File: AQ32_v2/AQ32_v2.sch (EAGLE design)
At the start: 115 parts, among them Q2 BCV27, Q3 BCV27, Q5 BCV27, Q6 BCV27, U1 ITG-3200, U10 MS5611, U11 MIC5239, U13 74AHC1G86DCK, U2 STM32F10XVXT6, U3 74AHC1G86DCK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

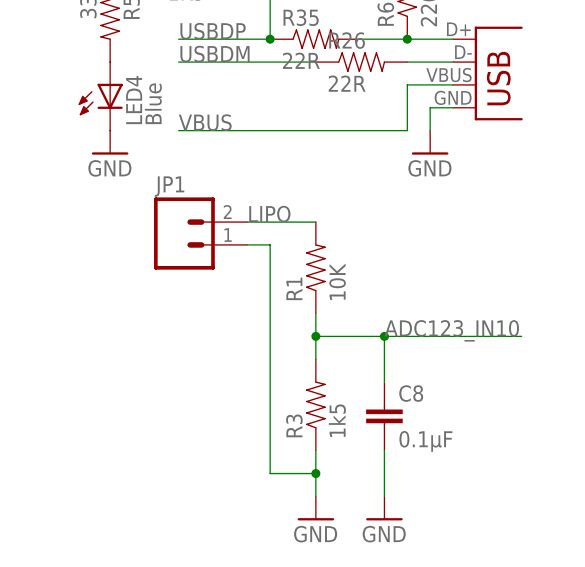
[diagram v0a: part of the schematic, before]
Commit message: reverted to fixed ground plane for BM and LED GND's, moved lavels
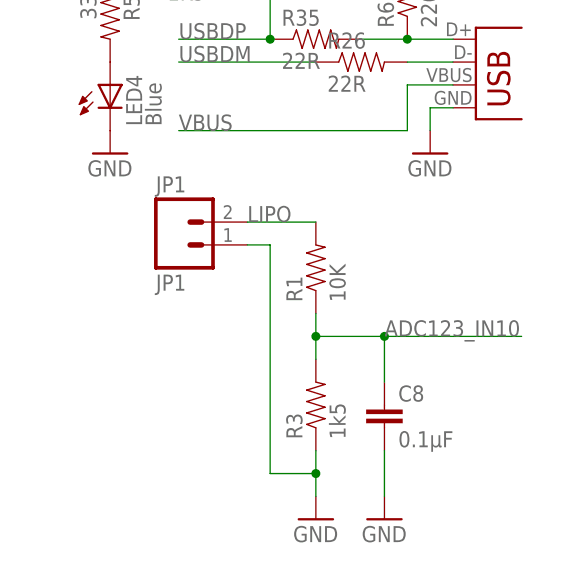
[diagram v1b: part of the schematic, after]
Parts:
- JP1: value (none) -> JP1; device SparkFun-Connectors:M02PTH -> SparkFun-Connectors:M02LOCK
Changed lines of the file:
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@@
 <part name="GND25" library="SparkFun" deviceset="GND" device=""/>
 <part name="SUPPLY2" library="supply2" deviceset="V+" device="" value="VDD"/>
-<part name="JP1" library="SparkFun-Connectors" deviceset="M02" device="PTH"/>
+<part name="JP1" library="SparkFun-Connectors" deviceset="M02" device="LOCK" value="JP1"/>
 </parts>
 <sheets>
@@
 <pinref part="R3" gate="G$1" pin="1"/>
 <pinref part="GND15" gate="1" pin="GND"/>
-<pinref part="JP1" gate="G$1" pin="1"/>
 <wire x1="33.02" y1="73.66" x2="33.02" y2="71.12" width="0.1524" layer="91"/>
 <wire x1="25.4" y1="99.06" x2="27.94" y2="99.06" width="0.1524" layer="91"/>
@@
 <wire x1="27.94" y1="73.66" x2="33.02" y2="73.66" width="0.1524" layer="91"/>
 <junction x="33.02" y="73.66"/>
-</segment>
-<segment>
+<pinref part="JP1" gate="G$1" pin="1"/>
+</segment>
+<segment>

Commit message: "j" version from Alfred
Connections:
- net 3V3AN: now also C29.1, C45.1, U1.VDD, U10.CSB, U10.CSB@2, U10.PS, U10.VDD; no longer I2C-1.S, JP1-2.7, JP1-2.8, SERIAL-1.S
- net 3V3DIG: now also I2C-1.S, JP1-2.7, JP1-2.8, SERIAL-1.S; no longer C29.1, C45.1, U1.VDD, U10.CSB, U10.CSB@2, U10.PS, U10.VDD
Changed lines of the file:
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@@
 <part name="U10" library="DSP-TI" deviceset="MS5611" device=""/>
 <part name="SUPPLY19" library="supply2" deviceset="GND" device=""/>
-<part name="SUPPLY20" library="supply2" deviceset="VDD" device=""/>
 <part name="C45" library="rcl" deviceset="C-US" device="C0402" value="0.1uF"/>
 <part name="SUPPLY21" library="supply2" deviceset="GND" device=""/>
@@
 <part name="SUPPLY2" library="supply2" deviceset="V+" device="" value="VDD"/>
 <part name="JP1" library="SparkFun-Connectors" deviceset="M02" device="LOCK" value="JP1"/>
+<part name="P+4" library="SparkFun" deviceset="3.3V" device="" value="VDDA"/>
 </parts>
 <sheets>
@@
 <instance part="U10" gate="G$1" x="307.34" y="33.02"/>
 <instance part="SUPPLY19" gate="GND" x="309.88" y="10.16"/>
-<instance part="SUPPLY20" gate="G$1" x="309.88" y="60.96"/>
 <instance part="C45" gate="G$1" x="325.12" y="50.8"/>
 <instance part="SUPPLY21" gate="GND" x="325.12" y="40.64"/>
@@
 <instance part="SUPPLY2" gate="1" x="129.54" y="60.96"/>
 <instance part="JP1" gate="G$1" x="17.78" y="99.06"/>
+<instance part="P+4" gate="G$1" x="309.88" y="58.42"/>
 </instances>
 <busses>
@@
 </segment>
 <segment>
-<pinref part="SERIAL" gate="-1" pin="S"/>
-<wire x1="86.36" y1="68.58" x2="76.2" y2="68.58" width="0.1524" layer="91"/>
-<label x="76.2" y="68.58" size="1.778" layer="95"/>
-</segment>
-<segment>
-<pinref part="I2C" gate="-1" pin="S"/>
-<wire x1="86.36" y1="83.82" x2="76.2" y2="83.82" width="0.1524" layer="91"/>
-<label x="76.2" y="83.82" size="1.778" layer="95"/>
-</segment>
-<segment>
-<pinref part="JP1-2" gate="G$1" pin="8"/>
-<wire x1="429.26" y1="76.2" x2="436.88" y2="76.2" width="0.1524" layer="91"/>
-<label x="429.26" y="76.2" size="1.778" layer="95"/>
-</segment>
-<segment>
-<pinref part="JP1-2" gate="G$1" pin="7"/>
-<wire x1="429.26" y1="73.66" x2="436.88" y2="73.66" width="0.1524" layer="91"/>
-<label x="429.26" y="73.66" size="1.778" layer="95"/>
+<wire x1="309.88" y1="58.42" x2="309.88" y2="55.88" width="0.1524" layer="91"/>
+<wire x1="309.88" y1="55.88" x2="309.88" y2="50.8" width="0.1524" layer="91"/>
+<wire x1="309.88" y1="55.88" x2="325.12" y2="55.88" width="0.1524" layer="91"/>
+<wire x1="325.12" y1="55.88" x2="325.12" y2="53.34" width="0.1524" layer="91"/>
+<junction x="309.88" y="55.88"/>
+<pinref part="U10" gate="G$1" pin="VDD"/>
+<pinref part="C45" gate="G$1" pin="1"/>
+<label x="309.88" y="58.42" size="1.778" layer="95"/>
+<wire x1="309.88" y1="55.88" x2="281.94" y2="55.88" width="0.1524" layer="91"/>
+<wire x1="281.94" y1="55.88" x2="281.94" y2="40.64" width="0.1524" layer="91"/>
+<pinref part="U10" gate="G$1" pin="CSB@2"/>
+<wire x1="281.94" y1="40.64" x2="281.94" y2="38.1" width="0.1524" layer="91"/>
+<wire x1="281.94" y1="38.1" x2="281.94" y2="35.56" width="0.1524" layer="91"/>
+<wire x1="281.94" y1="35.56" x2="292.1" y2="35.56" width="0.1524" layer="91"/>
+<pinref part="U10" gate="G$1" pin="CSB"/>
+<wire x1="292.1" y1="38.1" x2="281.94" y2="38.1" width="0.1524" layer="91"/>
+<pinref part="U10" gate="G$1" pin="PS"/>
+<wire x1="292.1" y1="40.64" x2="281.94" y2="40.64" width="0.1524" layer="91"/>
+<junction x="281.94" y="40.64"/>
+<junction x="281.94" y="38.1"/>
+<pinref part="P+4" gate="G$1" pin="3.3V"/>
+</segment>
+<segment>
+<wire x1="342.9" y1="157.48" x2="327.66" y2="157.48" width="0.1524" layer="91"/>
+<wire x1="342.9" y1="157.48" x2="342.9" y2="149.86" width="0.1524" layer="91"/>
+<junction x="327.66" y="157.48"/>
+<label x="330.2" y="157.48" size="1.778" layer="95"/>
+<pinref part="U1" gate="G$1" pin="VDD"/>
+<pinref part="C29" gate="G$1" pin="1"/>
 </segment>
 </net>
@@
 </segment>
 <segment>
-<wire x1="309.88" y1="58.42" x2="309.88" y2="55.88" width="0.1524" layer="91"/>
-<wire x1="309.88" y1="55.88" x2="309.88" y2="50.8" width="0.1524" layer="91"/>
-<wire x1="309.88" y1="55.88" x2="325.12" y2="55.88" width="0.1524" layer="91"/>
-<wire x1="325.12" y1="55.88" x2="325.12" y2="53.34" width="0.1524" layer="91"/>
-<junction x="309.88" y="55.88"/>
-<pinref part="SUPPLY20" gate="G$1" pin="VDD"/>
-<pinref part="U10" gate="G$1" pin="VDD"/>
-<pinref part="C45" gate="G$1" pin="1"/>
-<label x="309.88" y="58.42" size="1.778" layer="95"/>
-<wire x1="309.88" y1="55.88" x2="281.94" y2="55.88" width="0.1524" layer="91"/>
-<wire x1="281.94" y1="55.88" x2="281.94" y2="40.64" width="0.1524" layer="91"/>
-<pinref part="U10" gate="G$1" pin="CSB@2"/>
-<wire x1="281.94" y1="40.64" x2="281.94" y2="38.1" width="0.1524" layer="91"/>
-<wire x1="281.94" y1="38.1" x2="281.94" y2="35.56" width="0.1524" layer="91"/>
-<wire x1="281.94" y1="35.56" x2="292.1" y2="35.56" width="0.1524" layer="91"/>
-<pinref part="U10" gate="G$1" pin="CSB"/>
-<wire x1="292.1" y1="38.1" x2="281.94" y2="38.1" width="0.1524" layer="91"/>
-<pinref part="U10" gate="G$1" pin="PS"/>
-<wire x1="292.1" y1="40.64" x2="281.94" y2="40.64" width="0.1524" layer="91"/>
-<junction x="281.94" y="40.64"/>
-<junction x="281.94" y="38.1"/>
-</segment>
-<segment>
-<wire x1="342.9" y1="157.48" x2="327.66" y2="157.48" width="0.1524" layer="91"/>
-<wire x1="342.9" y1="157.48" x2="342.9" y2="149.86" width="0.1524" layer="91"/>
-<junction x="327.66" y="157.48"/>
-<label x="330.2" y="157.48" size="1.778" layer="95"/>
-<pinref part="U1" gate="G$1" pin="VDD"/>
-<pinref part="C29" gate="G$1" pin="1"/>
-</segment>
-<segment>
 <wire x1="261.62" y1="170.18" x2="261.62" y2="175.26" width="0.1524" layer="91"/>
 <label x="259.08" y="175.26" size="1.778" layer="95"/>
@@
 <label x="129.54" y="55.88" size="1.778" layer="95"/>
 </segment>
-</net>
+<segment>
+<pinref part="I2C" gate="-1" pin="S"/>
+<wire x1="86.36" y1="83.82" x2="76.2" y2="83.82" width="0.1524" layer="91"/>
+<label x="76.2" y="83.82" size="1.778" layer="95"/>
+</segment>
+<segment>
+<pinref part="SERIAL" gate="-1" pin="S"/>
+<wire x1="86.36" y1="68.58" x2="76.2" y2="68.58" width="0.1524" layer="91"/>
+<label x="76.2" y="68.58" size="1.778" layer="95"/>
+</segment>
+<segment>
+<pinref part="JP1-2" gate="G$1" pin="8"/>
+<wire x1="429.26" y1="76.2" x2="436.88" y2="76.2" width="0.1524" layer="91"/>
+<label x="429.26" y="76.2" size="1.778" layer="95"/>
+</segment>
+<segment>
+<pinref part="JP1-2" gate="G$1" pin="7"/>
+<wire x1="429.26" y1="73.66" x2="436.88" y2="73.66" width="0.1524" layer="91"/>
+<label x="429.26" y="73.66" size="1.778" layer="95"/>
+</segment>
+</net>

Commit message: Revert ""j" version from Alfred"
This reverts commit dfbd99c4a951c4a7fc19233cae0e41e3843b112f.
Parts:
- JP1: value JP1 -> (none); device SparkFun-Connectors:M02LOCK -> SparkFun-Connectors:M02PTH
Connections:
- net 3V3AN: now also I2C-1.S, JP1-2.7, JP1-2.8, SERIAL-1.S; no longer C29.1, C45.1, U1.VDD, U10.CSB, U10.CSB@2, U10.PS, U10.VDD
- net 3V3DIG: now also C29.1, C45.1, U1.VDD, U10.CSB, U10.CSB@2, U10.PS, U10.VDD; no longer I2C-1.S, JP1-2.7, JP1-2.8, SERIAL-1.S
- net LEDGND1: now also Q5.C; no longer Q2.C
- net LEDGND2: now also Q2.C; no longer Q5.C
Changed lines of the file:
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@@
 <part name="U10" library="DSP-TI" deviceset="MS5611" device=""/>
 <part name="SUPPLY19" library="supply2" deviceset="GND" device=""/>
+<part name="SUPPLY20" library="supply2" deviceset="VDD" device=""/>
 <part name="C45" library="rcl" deviceset="C-US" device="C0402" value="0.1uF"/>
 <part name="SUPPLY21" library="supply2" deviceset="GND" device=""/>
@@
 <part name="GND25" library="SparkFun" deviceset="GND" device=""/>
 <part name="SUPPLY2" library="supply2" deviceset="V+" device="" value="VDD"/>
-<part name="JP1" library="SparkFun-Connectors" deviceset="M02" device="LOCK" value="JP1"/>
-<part name="P+4" library="SparkFun" deviceset="3.3V" device="" value="VDDA"/>
+<part name="JP1" library="SparkFun-Connectors" deviceset="M02" device="PTH"/>
 </parts>
 <sheets>
@@
 <instance part="U10" gate="G$1" x="307.34" y="33.02"/>
 <instance part="SUPPLY19" gate="GND" x="309.88" y="10.16"/>
+<instance part="SUPPLY20" gate="G$1" x="309.88" y="60.96"/>
 <instance part="C45" gate="G$1" x="325.12" y="50.8"/>
 <instance part="SUPPLY21" gate="GND" x="325.12" y="40.64"/>
@@
 <instance part="SUPPLY2" gate="1" x="129.54" y="60.96"/>
 <instance part="JP1" gate="G$1" x="17.78" y="99.06"/>
-<instance part="P+4" gate="G$1" x="309.88" y="58.42"/>
 </instances>
 <busses>
@@
 <pinref part="R3" gate="G$1" pin="1"/>
 <pinref part="GND15" gate="1" pin="GND"/>
+<pinref part="JP1" gate="G$1" pin="1"/>
 <wire x1="33.02" y1="73.66" x2="33.02" y2="71.12" width="0.1524" layer="91"/>
 <wire x1="25.4" y1="99.06" x2="27.94" y2="99.06" width="0.1524" layer="91"/>
@@
 <wire x1="27.94" y1="73.66" x2="33.02" y2="73.66" width="0.1524" layer="91"/>
 <junction x="33.02" y="73.66"/>
-<pinref part="JP1" gate="G$1" pin="1"/>
 </segment>
 <segment>
@@
 </segment>
 <segment>
-<wire x1="309.88" y1="58.42" x2="309.88" y2="55.88" width="0.1524" layer="91"/>
-<wire x1="309.88" y1="55.88" x2="309.88" y2="50.8" width="0.1524" layer="91"/>
-<wire x1="309.88" y1="55.88" x2="325.12" y2="55.88" width="0.1524" layer="91"/>
-<wire x1="325.12" y1="55.88" x2="325.12" y2="53.34" width="0.1524" layer="91"/>
-<junction x="309.88" y="55.88"/>
-<pinref part="U10" gate="G$1" pin="VDD"/>
-<pinref part="C45" gate="G$1" pin="1"/>
-<label x="309.88" y="58.42" size="1.778" layer="95"/>
-<wire x1="309.88" y1="55.88" x2="281.94" y2="55.88" width="0.1524" layer="91"/>
-<wire x1="281.94" y1="55.88" x2="281.94" y2="40.64" width="0.1524" layer="91"/>
-<pinref part="U10" gate="G$1" pin="CSB@2"/>
-<wire x1="281.94" y1="40.64" x2="281.94" y2="38.1" width="0.1524" layer="91"/>
-<wire x1="281.94" y1="38.1" x2="281.94" y2="35.56" width="0.1524" layer="91"/>
-<wire x1="281.94" y1="35.56" x2="292.1" y2="35.56" width="0.1524" layer="91"/>
-<pinref part="U10" gate="G$1" pin="CSB"/>
-<wire x1="292.1" y1="38.1" x2="281.94" y2="38.1" width="0.1524" layer="91"/>
-<pinref part="U10" gate="G$1" pin="PS"/>
-<wire x1="292.1" y1="40.64" x2="281.94" y2="40.64" width="0.1524" layer="91"/>
-<junction x="281.94" y="40.64"/>
-<junction x="281.94" y="38.1"/>
-<pinref part="P+4" gate="G$1" pin="3.3V"/>
-</segment>
-<segment>
-<wire x1="342.9" y1="157.48" x2="327.66" y2="157.48" width="0.1524" layer="91"/>
-<wire x1="342.9" y1="157.48" x2="342.9" y2="149.86" width="0.1524" layer="91"/>
-<junction x="327.66" y="157.48"/>
-<label x="330.2" y="157.48" size="1.778" layer="95"/>
-<pinref part="U1" gate="G$1" pin="VDD"/>
-<pinref part="C29" gate="G$1" pin="1"/>
+<pinref part="SERIAL" gate="-1" pin="S"/>
+<wire x1="86.36" y1="68.58" x2="76.2" y2="68.58" width="0.1524" layer="91"/>
+<label x="76.2" y="68.58" size="1.778" layer="95"/>
+</segment>
+<segment>
+<pinref part="I2C" gate="-1" pin="S"/>
+<wire x1="86.36" y1="83.82" x2="76.2" y2="83.82" width="0.1524" layer="91"/>
+<label x="76.2" y="83.82" size="1.778" layer="95"/>
+</segment>
+<segment>
+<pinref part="JP1-2" gate="G$1" pin="8"/>
+<wire x1="429.26" y1="76.2" x2="436.88" y2="76.2" width="0.1524" layer="91"/>
+<label x="429.26" y="76.2" size="1.778" layer="95"/>
+</segment>
+<segment>
+<pinref part="JP1-2" gate="G$1" pin="7"/>
+<wire x1="429.26" y1="73.66" x2="436.88" y2="73.66" width="0.1524" layer="91"/>
+<label x="429.26" y="73.66" size="1.778" layer="95"/>
 </segment>
 </net>
@@
 </segment>
 <segment>
+<wire x1="309.88" y1="58.42" x2="309.88" y2="55.88" width="0.1524" layer="91"/>
+<wire x1="309.88" y1="55.88" x2="309.88" y2="50.8" width="0.1524" layer="91"/>
+<wire x1="309.88" y1="55.88" x2="325.12" y2="55.88" width="0.1524" layer="91"/>
+<wire x1="325.12" y1="55.88" x2="325.12" y2="53.34" width="0.1524" layer="91"/>
+<junction x="309.88" y="55.88"/>
+<pinref part="SUPPLY20" gate="G$1" pin="VDD"/>
+<pinref part="U10" gate="G$1" pin="VDD"/>
+<pinref part="C45" gate="G$1" pin="1"/>
+<label x="309.88" y="58.42" size="1.778" layer="95"/>
+<wire x1="309.88" y1="55.88" x2="281.94" y2="55.88" width="0.1524" layer="91"/>
+<wire x1="281.94" y1="55.88" x2="281.94" y2="40.64" width="0.1524" layer="91"/>
+<pinref part="U10" gate="G$1" pin="CSB@2"/>
+<wire x1="281.94" y1="40.64" x2="281.94" y2="38.1" width="0.1524" layer="91"/>
+<wire x1="281.94" y1="38.1" x2="281.94" y2="35.56" width="0.1524" layer="91"/>
+<wire x1="281.94" y1="35.56" x2="292.1" y2="35.56" width="0.1524" layer="91"/>
+<pinref part="U10" gate="G$1" pin="CSB"/>
+<wire x1="292.1" y1="38.1" x2="281.94" y2="38.1" width="0.1524" layer="91"/>
+<pinref part="U10" gate="G$1" pin="PS"/>
+<wire x1="292.1" y1="40.64" x2="281.94" y2="40.64" width="0.1524" layer="91"/>
+<junction x="281.94" y="40.64"/>
+<junction x="281.94" y="38.1"/>
+</segment>
+<segment>
+<wire x1="342.9" y1="157.48" x2="327.66" y2="157.48" width="0.1524" layer="91"/>
+<wire x1="342.9" y1="157.48" x2="342.9" y2="149.86" width="0.1524" layer="91"/>
+<junction x="327.66" y="157.48"/>
+<label x="330.2" y="157.48" size="1.778" layer="95"/>
+<pinref part="U1" gate="G$1" pin="VDD"/>
+<pinref part="C29" gate="G$1" pin="1"/>
+</segment>
+<segment>
 <wire x1="261.62" y1="170.18" x2="261.62" y2="175.26" width="0.1524" layer="91"/>
 <label x="259.08" y="175.26" size="1.778" layer="95"/>
@@
 <pinref part="U3" gate="P" pin="VCC"/>
 <label x="129.54" y="55.88" size="1.778" layer="95"/>
-</segment>
-<segment>
-<pinref part="I2C" gate="-1" pin="S"/>
-<wire x1="86.36" y1="83.82" x2="76.2" y2="83.82" width="0.1524" layer="91"/>
-<label x="76.2" y="83.82" size="1.778" layer="95"/>
-</segment>
-<segment>
-<pinref part="SERIAL" gate="-1" pin="S"/>
-<wire x1="86.36" y1="68.58" x2="76.2" y2="68.58" width="0.1524" layer="91"/>
-<label x="76.2" y="68.58" size="1.778" layer="95"/>
-</segment>
-<segment>
-<pinref part="JP1-2" gate="G$1" pin="8"/>
-<wire x1="429.26" y1="76.2" x2="436.88" y2="76.2" width="0.1524" layer="91"/>
-<label x="429.26" y="76.2" size="1.778" layer="95"/>
-</segment>
-<segment>
-<pinref part="JP1-2" gate="G$1" pin="7"/>
-<wire x1="429.26" y1="73.66" x2="436.88" y2="73.66" width="0.1524" layer="91"/>
-<label x="429.26" y="73.66" size="1.778" layer="95"/>
 </segment>
 </net>
@@
 <net name="LEDGND1" class="0">
 <segment>
+<wire x1="30.48" y1="45.72" x2="27.94" y2="45.72" width="0.1524" layer="91"/>
+<pinref part="Q5" gate="G$1" pin="C"/>
+<label x="27.94" y="45.72" size="1.778" layer="95"/>
+</segment>
+<segment>
 <pinref part="JP4-1" gate="G$1" pin="1"/>
 <wire x1="495.3" y1="25.4" x2="505.46" y2="25.4" width="0.1524" layer="91"/>
 <label x="495.3" y="25.4" size="1.778" layer="95"/>
 </segment>
+</net>
+<net name="LEDGND2" class="0">
 <segment>
 <wire x1="30.48" y1="33.02" x2="27.94" y2="33.02" width="0.1524" layer="91"/>
@@
 <label x="27.94" y="33.02" size="1.778" layer="95"/>
 </segment>
-</net>
-<net name="LEDGND2" class="0">
 <segment>
 <pinref part="JP4-1" gate="G$1" pin="2"/>
@@
 <label x="495.3" y="27.94" size="1.778" layer="95"/>
 </segment>
-<segment>
-<wire x1="30.48" y1="45.72" x2="27.94" y2="45.72" width="0.1524" layer="91"/>
-<pinref part="Q5" gate="G$1" pin="C"/>
-<label x="27.94" y="45.72" size="1.778" layer="95"/>
-</segment>
-</net>
+</net>
